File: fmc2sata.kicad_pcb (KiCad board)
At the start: 4 copper layers, 108 x 69 mm, 58 parts, among them J1 ASP-134488-01, J2 1-2199230-6, J3 te-770829-1, Q1 BSS138APW, Q2 BSS138APW, Q3 DMG2305UX-13, Q4 BSS138APW, U1 TPS565208, U2 TPS565208, Y1 AX3DAF1-150.0000

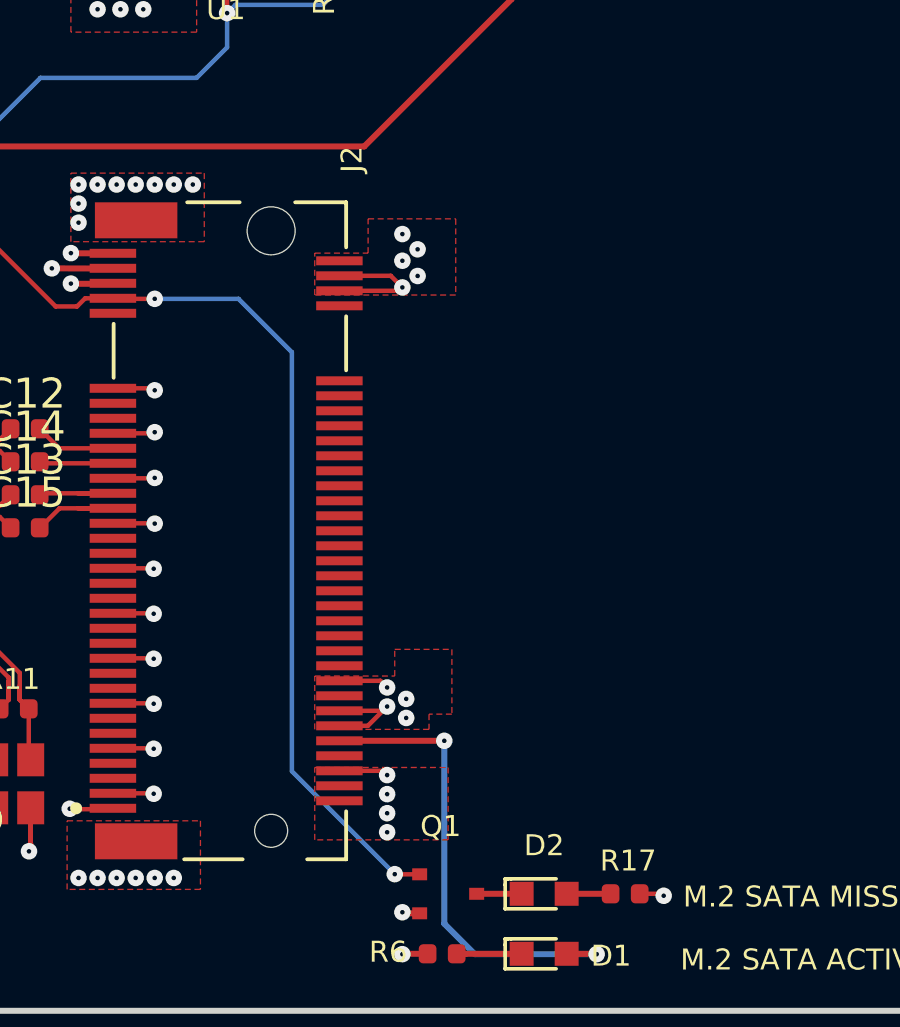
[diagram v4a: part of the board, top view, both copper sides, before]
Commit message: Add filtering caps
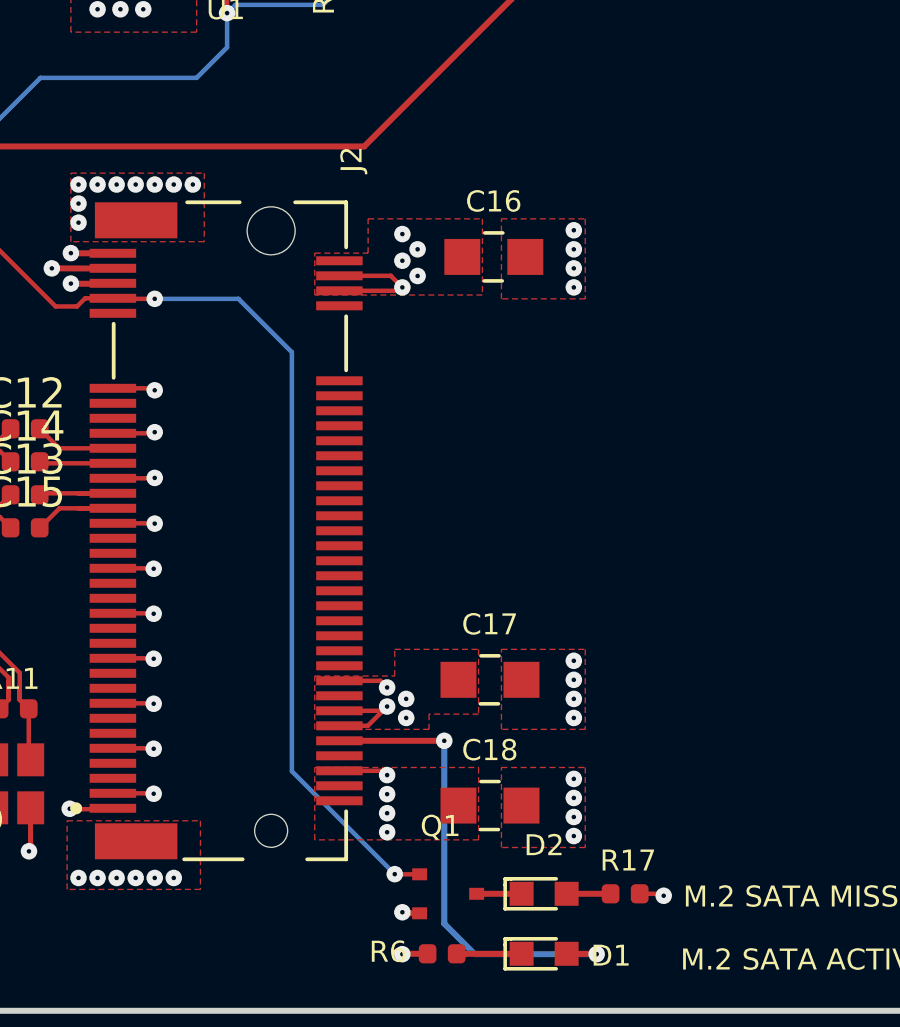
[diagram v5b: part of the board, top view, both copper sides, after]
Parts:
- added C16: C_22u_0805_10V, fmc2sata-footprints:0805-cap, F.Cu at (104.2, 86.9)
- added C17: C_22u_0805_10V, fmc2sata-footprints:0805-cap, F.Cu at (104.1, 101.0)
- added C18: C_22u_0805_10V, fmc2sata-footprints:0805-cap, F.Cu at (104.1, 105.2)
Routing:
- net GND: vias 144 -> 156
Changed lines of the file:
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@@
     (thickness 1.6)
     (drawings 13)
-    (tracks 971)
+    (tracks 983)
     (zones 0)
-    (modules 58)
+    (modules 61)
     (nets 163)
   )
@@
     (add_net SATA_CLK_P)
   )
+  (module fmc2sata-footprints:0805-cap (layer F.Cu)
+    (at 104.095 105.159)
+    (attr smd)
+    (fp_text reference C18 (at 0 -1.84) (layer F.SilkS)
+      (effects (font (size 0.7 0.7) (thickness 0.15)))
+    )
+    (fp_text value C_22u_0805_10V (at 0 1.95) (layer F.Fab)
+      (effects (font (size 1 1) (thickness 0.15)))
+    )
+    (fp_line (start -0.95 -0.675) (end -0.95 0.675) (layer F.Fab) (width 0.12))
+    (fp_line (start 0.95 -0.675) (end 0.95 0.675) (layer F.Fab) (width 0.12))
+    (fp_line (start -0.95 -0.68) (end 0.95 -0.68) (layer F.Fab) (width 0.12))
+    (fp_line (start -0.95 0.68) (end 0.95 0.68) (layer F.Fab) (width 0.12))
+    (fp_line (start -0.3 -0.8) (end 0.3 -0.8) (layer F.SilkS) (width 0.12))
+    (fp_line (start -0.32 0.8) (end 0.28 0.8) (layer F.SilkS) (width 0.12))
+    (fp_line (start -1.9 0.93) (end -1.9 -0.93) (layer F.CrtYd) (width 0.05))
+    (fp_line (start 1.9 0.93) (end 1.9 -0.93) (layer F.CrtYd) (width 0.05))
+    (fp_line (start -1.9 -0.93) (end 1.9 -0.93) (layer F.CrtYd) (width 0.05))
+    (fp_line (start -1.9 0.93) (end 1.9 0.93) (layer F.CrtYd) (width 0.05))
+    (pad 1 smd rect (at -1.05 0) (size 1.2 1.2) (layers F.Cu F.Paste F.Mask)
+      (net 132 +3V3))
+    (pad 2 smd rect (at 1.05 0) (size 1.2 1.2) (layers F.Cu F.Paste F.Mask)
+      (net 2 GND))
+    (model ${KIPRJMOD}/lib/3d-models/0805-cap.step
+      (offset (xyz -1 0.7 1.2))
+      (scale (xyz 1 1 1))
+      (rotate (xyz 90 0 0))
+    )
+  )
+  (module fmc2sata-footprints:0805-cap (layer F.Cu)
+    (at 104.095 100.968)
+    (attr smd)
+    (fp_text reference C17 (at 0 -1.84) (layer F.SilkS)
+      (effects (font (size 0.7 0.7) (thickness 0.15)))
+    )
+    (fp_text value C_22u_0805_10V (at 0 1.95) (layer F.Fab)
+      (effects (font (size 1 1) (thickness 0.15)))
+    )
+    (fp_line (start -0.95 -0.675) (end -0.95 0.675) (layer F.Fab) (width 0.12))
+    (fp_line (start 0.95 -0.675) (end 0.95 0.675) (layer F.Fab) (width 0.12))
+    (fp_line (start -0.95 -0.68) (end 0.95 -0.68) (layer F.Fab) (width 0.12))
+    (fp_line (start -0.95 0.68) (end 0.95 0.68) (layer F.Fab) (width 0.12))
+    (fp_line (start -0.3 -0.8) (end 0.3 -0.8) (layer F.SilkS) (width 0.12))
+    (fp_line (start -0.32 0.8) (end 0.28 0.8) (layer F.SilkS) (width 0.12))
+    (fp_line (start -1.9 0.93) (end -1.9 -0.93) (layer F.CrtYd) (width 0.05))
+    (fp_line (start 1.9 0.93) (end 1.9 -0.93) (layer F.CrtYd) (width 0.05))
+    (fp_line (start -1.9 -0.93) (end 1.9 -0.93) (layer F.CrtYd) (width 0.05))
+    (fp_line (start -1.9 0.93) (end 1.9 0.93) (layer F.CrtYd) (width 0.05))
+    (pad 1 smd rect (at -1.05 0) (size 1.2 1.2) (layers F.Cu F.Paste F.Mask)
+      (net 132 +3V3))
+    (pad 2 smd rect (at 1.05 0) (size 1.2 1.2) (layers F.Cu F.Paste F.Mask)
+      (net 2 GND))
+    (model ${KIPRJMOD}/lib/3d-models/0805-cap.step
+      (offset (xyz -1 0.7 1.2))
+      (scale (xyz 1 1 1))
+      (rotate (xyz 90 0 0))
+    )
+  )
+  (module fmc2sata-footprints:0805-cap (layer F.Cu)
+    (at 104.222 86.871)
+    (attr smd)
+    (fp_text reference C16 (at 0 -1.84) (layer F.SilkS)
+      (effects (font (size 0.7 0.7) (thickness 0.15)))
+    )
+    (fp_text value C_22u_0805_10V (at 0 1.95) (layer F.Fab)
+      (effects (font (size 1 1) (thickness 0.15)))
+    )
+    (fp_line (start -0.95 -0.675) (end -0.95 0.675) (layer F.Fab) (width 0.12))
+    (fp_line (start 0.95 -0.675) (end 0.95 0.675) (layer F.Fab) (width 0.12))
+    (fp_line (start -0.95 -0.68) (end 0.95 -0.68) (layer F.Fab) (width 0.12))
+    (fp_line (start -0.95 0.68) (end 0.95 0.68) (layer F.Fab) (width 0.12))
+    (fp_line (start -0.3 -0.8) (end 0.3 -0.8) (layer F.SilkS) (width 0.12))
+    (fp_line (start -0.32 0.8) (end 0.28 0.8) (layer F.SilkS) (width 0.12))
+    (fp_line (start -1.9 0.93) (end -1.9 -0.93) (layer F.CrtYd) (width 0.05))
+    (fp_line (start 1.9 0.93) (end 1.9 -0.93) (layer F.CrtYd) (width 0.05))
+    (fp_line (start -1.9 -0.93) (end 1.9 -0.93) (layer F.CrtYd) (width 0.05))
+    (fp_line (start -1.9 0.93) (end 1.9 0.93) (layer F.CrtYd) (width 0.05))
+    (pad 1 smd rect (at -1.05 0) (size 1.2 1.2) (layers F.Cu F.Paste F.Mask)
+      (net 132 +3V3))
+    (pad 2 smd rect (at 1.05 0) (size 1.2 1.2) (layers F.Cu F.Paste F.Mask)
+      (net 2 GND))
+    (model ${KIPRJMOD}/lib/3d-models/0805-cap.step
+      (offset (xyz -1 0.7 1.2))
+      (scale (xyz 1 1 1))
+      (rotate (xyz 90 0 0))
+    )
+  )
   (module fmc2sata-footprints:ASP-134488-01 (layer B.Cu)
     (at 80.6 77.6 270)
@@
   (segment (start 82.782 102.873) (end 82.782 103.485) (width 0.15) (layer F.Cu) (net 2))
   (segment (start 82.782 103.485) (end 82.759 103.508) (width 0.15) (layer F.Cu) (net 2))
+  (via (at 106.889 104.27) (size 0.55) (drill 0.15) (layers F.Cu B.Cu) (net 2))
+  (via (at 106.889 104.905) (size 0.55) (drill 0.15) (layers F.Cu B.Cu) (net 2))
+  (via (at 106.889 105.54) (size 0.55) (drill 0.15) (layers F.Cu B.Cu) (net 2))
+  (via (at 106.889 106.175) (size 0.55) (drill 0.15) (layers F.Cu B.Cu) (net 2))
+  (via (at 106.889 100.333) (size 0.55) (drill 0.15) (layers F.Cu B.Cu) (net 2))
+  (via (at 106.889 100.968) (size 0.55) (drill 0.15) (layers F.Cu B.Cu) (net 2))
+  (via (at 106.889 101.603) (size 0.55) (drill 0.15) (layers F.Cu B.Cu) (net 2))
+  (via (at 106.889 102.238) (size 0.55) (drill 0.15) (layers F.Cu B.Cu) (net 2))
+  (via (at 106.889 85.982) (size 0.55) (drill 0.15) (layers F.Cu B.Cu) (net 2))
+  (via (at 106.889 86.617) (size 0.55) (drill 0.15) (layers F.Cu B.Cu) (net 2))
+  (via (at 106.889 87.252) (size 0.55) (drill 0.15) (layers F.Cu B.Cu) (net 2))
+  (via (at 106.889 87.887) (size 0.55) (drill 0.15) (layers F.Cu B.Cu) (net 2))
   (segment (start 94.85 76.03) (end 93.85 76.03) (width 0.5) (layer F.Cu) (net 3))
   (segment (start 95.16 75.72) (end 94.85 76.03) (width 0.5) (layer F.Cu) (net 3))
@@
     (polygon
       (pts
-        (xy 102.952 88.141) (xy 98.253 88.141) (xy 98.253 86.744) (xy 100.031 86.744) (xy 100.031 85.601)
-        (xy 102.952 85.601)
+        (xy 103.841 88.141) (xy 98.253 88.141) (xy 98.253 86.744) (xy 100.031 86.744) (xy 100.031 85.601)
+        (xy 103.841 85.601)
       )
     )
@@
     (polygon
       (pts
-        (xy 102.825 102.111) (xy 102.063 102.111) (xy 102.063 102.619) (xy 98.253 102.619) (xy 98.253 100.841)
-        (xy 100.92 100.841) (xy 100.92 99.952) (xy 102.825 99.952)
+        (xy 103.714 102.111) (xy 102.063 102.111) (xy 102.063 102.619) (xy 98.253 102.619) (xy 98.253 100.841)
+        (xy 100.92 100.841) (xy 100.92 99.952) (xy 103.714 99.952)
       )
     )
@@
     (polygon
       (pts
-        (xy 102.698 106.302) (xy 98.253 106.302) (xy 98.253 103.889) (xy 102.698 103.889)
+        (xy 103.714 106.302) (xy 98.253 106.302) (xy 98.253 103.889) (xy 103.714 103.889)
       )
     )
@@
       )
     )
+  )
+  (zone (net 2) (net_name GND) (layer F.Cu) (hatch edge 0.508)
+    (connect_pads yes (clearance 0.25))
+    (min_thickness 0.254)
+    (fill yes (arc_segments 32) (thermal_gap 0.508) (thermal_bridge_width 0.508))
+    (polygon
+      (pts
+        (xy 107.27 106.556) (xy 104.476 106.556) (xy 104.476 103.889) (xy 107.27 103.889)
+      )
+    )
+  )
+  (zone (net 2) (net_name GND) (layer F.Cu) (hatch edge 0.508)
+    (connect_pads yes (clearance 0.25))
+    (min_thickness 0.254)
+    (fill yes (arc_segments 32) (thermal_gap 0.508) (thermal_bridge_width 0.508))
+    (polygon
+      (pts
+        (xy 107.27 102.619) (xy 104.476 102.619) (xy 104.476 99.952) (xy 107.27 99.952)
+      )
+    )
+  )
+  (zone (net 2) (net_name GND) (layer F.Cu) (hatch edge 0.508)
+    (connect_pads yes (clearance 0.25))
+    (min_thickness 0.254)
+    (fill yes (arc_segments 32) (thermal_gap 0.508) (thermal_bridge_width 0.508))
+    (polygon
+      (pts
+        (xy 107.27 88.268) (xy 104.476 88.268) (xy 104.476 85.601) (xy 107.27 85.601)
+      )
+    )
